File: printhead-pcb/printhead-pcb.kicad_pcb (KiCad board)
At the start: 2 copper layers, 35 x 35 mm, 61 parts, among them J1 PWR, J10 BL_TOUCH, J2 FAN0, J3 FAN2, J4 FAN1, J5 FAN3, J6 T0, J7 T1, J8 T2, J9 T3, Q1 DTC143E, Q2 DTC143E, Q3 DTC143E, Q4 DTC143E, U1 EMC2302-2-AIZL-TR, U2 EMC2302-2-AIZL-TR, U3 ADS1015IDGS, U4 PCA9536D

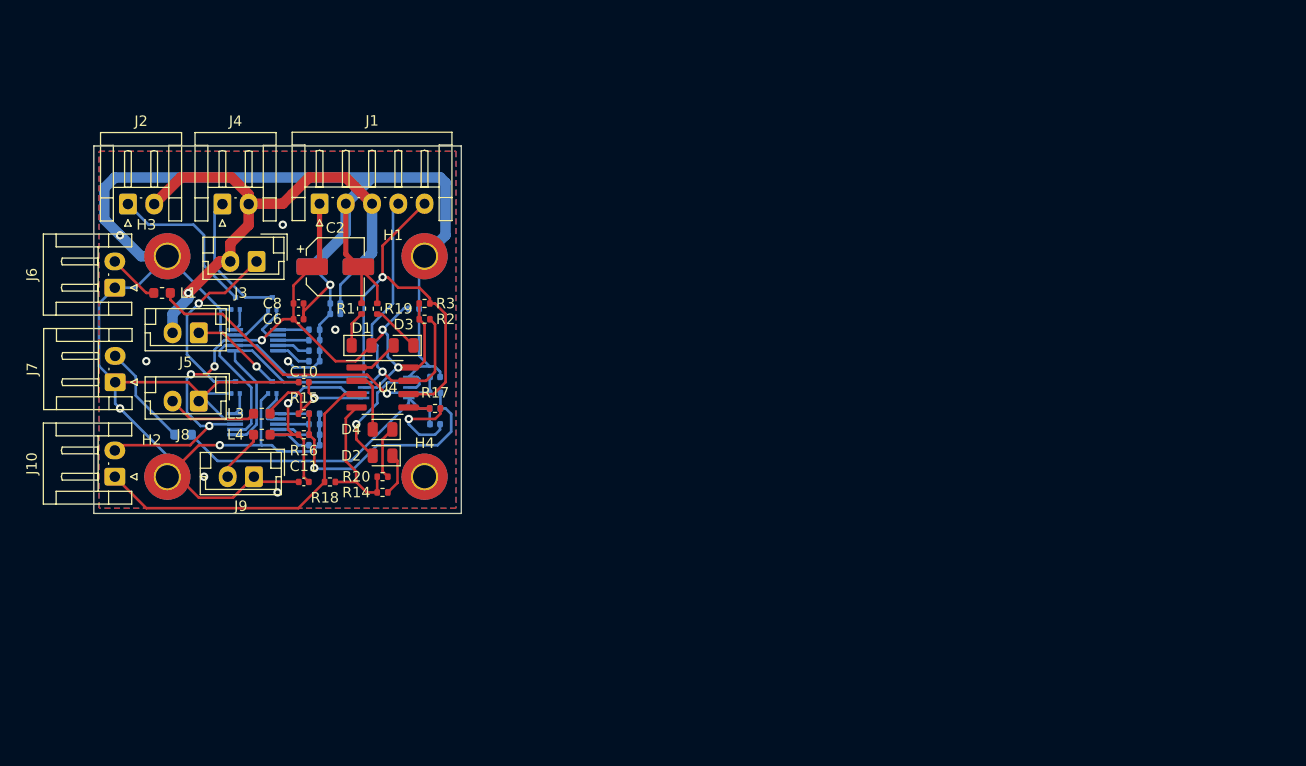
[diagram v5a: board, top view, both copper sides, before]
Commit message: removed led driver, added RJ45 (data connector), fan 3. 4. on off
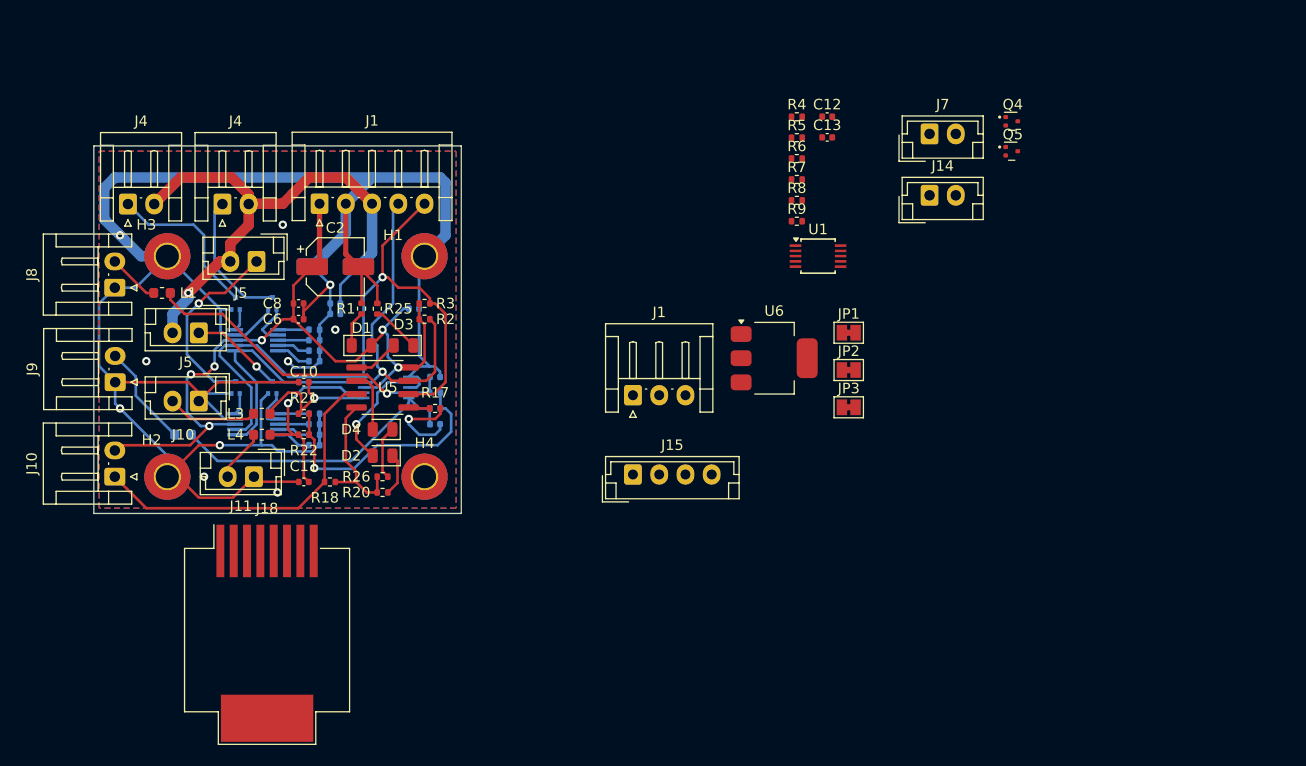
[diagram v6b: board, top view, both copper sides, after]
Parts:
- added C12: 4.7µF, Capacitor_SMD:C_0402_1005Metric, F.Cu at (176.3, 45.7)
- added C13: 4.7µF, Capacitor_SMD:C_0402_1005Metric, F.Cu at (176.3, 47.7)
- added J1: Power, Connector_JST:JST_EH_S3B-EH_1x03_P2.50mm_Horizontal, F.Cu at (157.8, 72.2)
- added J14: FAN4, Connector_JST:JST_EH_B2B-EH-A_1x02_P2.50mm_Vertical, F.Cu at (186.1, 53.2)
- added J15: BreakoutBoardADXL345, Connector_JST:JST_EH_B4B-EH-A_1x04_P2.50mm_Vertical, F.Cu at (157.8, 79.8)
- added J18: DATA, Connector_RJ:RJ45_Molex_0855135013_Vertical, F.Cu at (123.0, 94.9)
- added J7: FAN3, Connector_JST:JST_EH_B2B-EH-A_1x02_P2.50mm_Vertical, F.Cu at (186.1, 47.4)
- added JP1: MEASO, Jumper:SolderJumper-2_P1.3mm_Bridged_Pad1.0x1.5mm, F.Cu at (178.4, 66.3)
- added JP2: MEASO, Jumper:SolderJumper-2_P1.3mm_Bridged_Pad1.0x1.5mm, F.Cu at (178.4, 69.8)
- added JP3: MEASO, Jumper:SolderJumper-2_P1.3mm_Bridged_Pad1.0x1.5mm, F.Cu at (178.4, 73.4)
- added Q4: DTC143E, Package_TO_SOT_SMD:SOT-723, F.Cu at (193.9, 46.1)
- added Q5: DTC143E, Package_TO_SOT_SMD:SOT-723, F.Cu at (193.9, 49.0)
- added R4: 600, Resistor_SMD:R_0402_1005Metric, F.Cu at (173.5, 45.7)
- added R5: 120, Resistor_SMD:R_0402_1005Metric, F.Cu at (173.5, 47.7)
- added R6: 600, Resistor_SMD:R_0402_1005Metric, F.Cu at (173.5, 49.7)
- added R7: 600, Resistor_SMD:R_0402_1005Metric, F.Cu at (173.5, 51.7)
- added R8: 120, Resistor_SMD:R_0402_1005Metric, F.Cu at (173.5, 53.7)
- added R9: 600, Resistor_SMD:R_0402_1005Metric, F.Cu at (173.5, 55.7)
- added U1: PCA9615DP, Package_SO:TSSOP-10_3x3mm_P0.5mm, F.Cu at (175.5, 59.0)
- added U6: AP7361C-33E, Package_TO_SOT_SMD:SOT-223-3_TabPin2, F.Cu at (171.3, 68.7)
- R10: renamed from R4; value 10k -> 4k7
- R14: renamed from R8; value 10k -> 4k7
- R16: renamed from R10; value 10k -> 4k7
- R2, R3: value 10k -> 4k7
- renumbered J8 to J10, J9 to J11, J2 to J4, J3 to J5, J6 to J8, J7 to J9, R6 to R12, R12 to R18, R13 to R19, R14 to R20, R15 to R21, R16 to R22, R19 to R25, R20 to R26, U1 to U2, U3 to U4, U4 to U5
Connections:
- C2 pad 1: +3V3 -> +5V
- C4 pad 1: +3V3 -> +5V
- C6 pad 1: +3V3 -> +5V
- C8 pad 1: +3V3 -> +3.3V
- D1 pad 2: +3V3 -> +5V
- J10 pad 2: TC2 -> ADC2
- J11 pad 2: TC3 -> ADC3
- J4 pad 1: Net-(J2-Pin_1) -> Net-(J4-Pin_1)
- J5 pad 1: Net-(J3-Pin_1) -> Net-(J5-Pin_1)
- J8 pad 2: TC0 -> ADC0
- J9 pad 2: TC1 -> ADC1
- Q1 pad 3: Net-(J2-Pin_1) -> Net-(J4-Pin_1)
- Q2 pad 1: FAN_2_PWM -> FAN_1_PWM
- Q2 pad 3: Net-(J3-Pin_1) -> Net-(J5-Pin_1)
- R10 pad 1: Net-(U1-TACH1) -> Net-(U2-TACH1)
- R12 pad 1: Net-(U1-*ALERT) -> Net-(U2-*ALERT)
- R14 pad 1: Net-(U1-TACH2) -> Net-(U2-TACH2)
- R16 pad 1: Net-(U1-CLK) -> Net-(U2-CLK)
- R2 pad 1: +3V3 -> +5V
- R3 pad 1: +3V3 -> +5V
- U2 pad 10: Net-(U1-*ALERT) -> Net-(U2-*ALERT)
- U2 pad 6: Net-(U1-TACH1) -> Net-(U2-TACH1)
- U2 pad 8: Net-(U1-TACH2) -> Net-(U2-TACH2)
- U2 pad 9: Net-(U1-CLK) -> Net-(U2-CLK)
- U4 pad 8: +3V3 -> +3.3V
- U5 pad 8: +3V3 -> +3.3V
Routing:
- net Net-(J5-Pin_1): track 8.92 -> 27.1 mm, vias 1 -> 2
- net Net-(J3-Pin_1): track 18.2 -> 0.00 mm, vias 1 -> 0
- net Net-(J4-Pin_1): track 13.0 -> 28.6 mm
- net Net-(J2-Pin_1): track 15.6 -> 0.00 mm
- net Net-(U2-*ALERT): track 3.36 -> 6.72 mm
- net Net-(U1-*ALERT): track 3.36 -> 0.00 mm
- net Net-(U2-CLK): track 3.15 -> 6.30 mm
- net Net-(U1-CLK): track 3.15 -> 0.00 mm
- net Net-(U2-TACH1): track 2.95 -> 5.89 mm
- net Net-(U1-TACH1): track 2.95 -> 0.00 mm
- net Net-(U2-TACH2): track 2.95 -> 5.89 mm
- net Net-(U1-TACH2): track 2.95 -> 0.00 mm

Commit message: implemented custom footprint
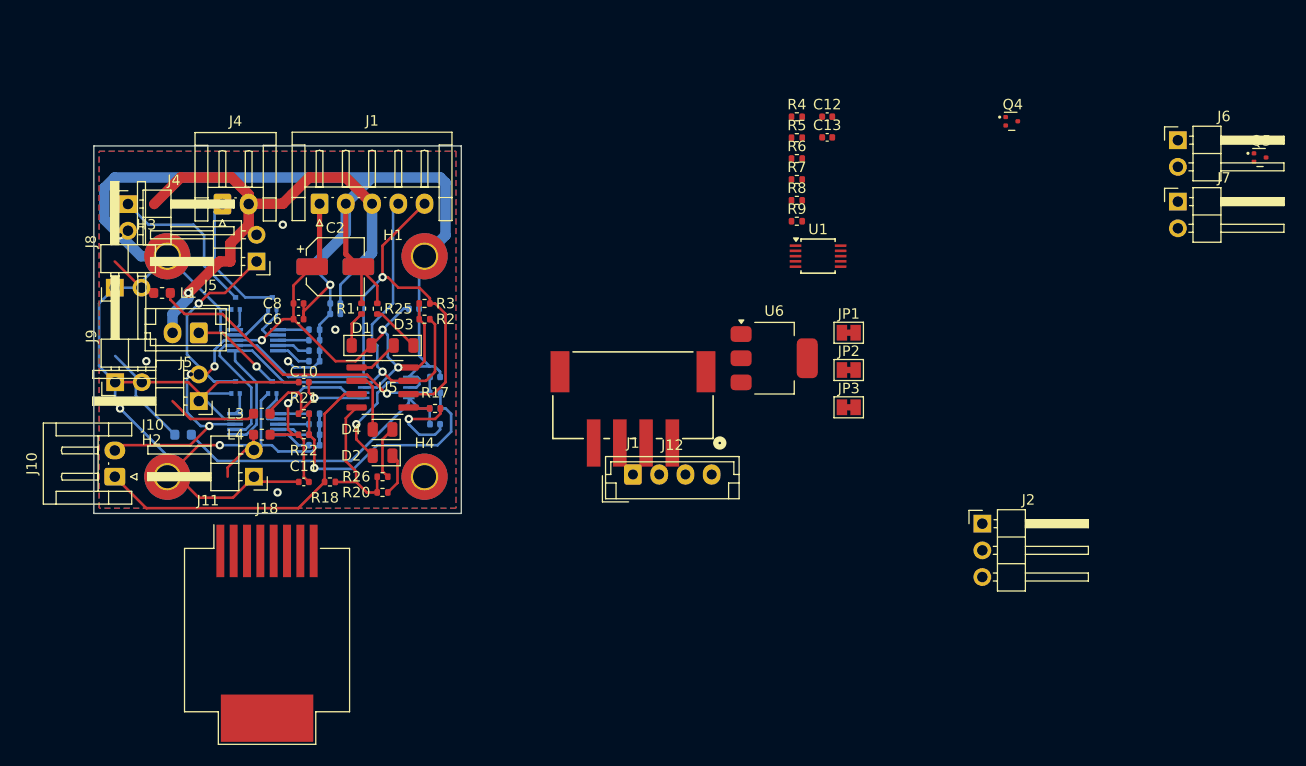
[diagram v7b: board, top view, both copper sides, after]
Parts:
- added J2: Fan_12/5V_Regelung, Connector_PinHeader_2.54mm:PinHeader_1x03_P2.54mm_Horizontal, F.Cu at (191.1, 84.5)
- C10: value 0.1µFC -> 0.1µF
- J1: footprint Connector_JST:JST_EH_S3B-EH_1x03_P2.50mm_Horizontal -> CustomFotLibByJan:CONN4_S4B-XH_JST
- J10, J11: footprint Connector_JST:JST_EH_B2B-EH-A_1x02_P2.50mm_Vertical -> Connector_PinHeader_2.54mm:PinHeader_1x02_P2.54mm_Horizontal
- J12: renamed from J15; value BreakoutBoardADXL345 -> Breakout_Board_ADXL345
- J4, J8, J9: footprint Connector_JST:JST_EH_S2B-EH_1x02_P2.50mm_Horizontal -> Connector_PinHeader_2.54mm:PinHeader_1x02_P2.54mm_Horizontal
- J5: value FAN2 -> FAN1; footprint Connector_JST:JST_EH_B2B-EH-A_1x02_P2.50mm_Vertical -> Connector_PinHeader_2.54mm:PinHeader_1x02_P2.54mm_Horizontal
- J6: renamed from J7; value FAN3 -> FAN2; footprint Connector_JST:JST_EH_B2B-EH-A_1x02_P2.50mm_Vertical -> Connector_PinHeader_2.54mm:PinHeader_1x02_P2.54mm_Horizontal
- J7: renamed from J14; footprint Connector_JST:JST_EH_B2B-EH-A_1x02_P2.50mm_Vertical -> Connector_PinHeader_2.54mm:PinHeader_1x02_P2.54mm_Horizontal
- moved J6 23.7 mm to (209.8, 48.0)
- moved J7 23.7 mm to (209.8, 53.8)
- moved Q5 23.7 mm to (217.6, 49.6)
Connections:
- J4 pad 2: +12V -> Fan_Versorgung
- J5 pad 2: +12V -> Fan_Versorgung
- J6 pad 2: +12V -> Fan_Versorgung
- J7 pad 2: +12V -> Fan_Versorgung

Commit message: added new sheet for stacked pcb
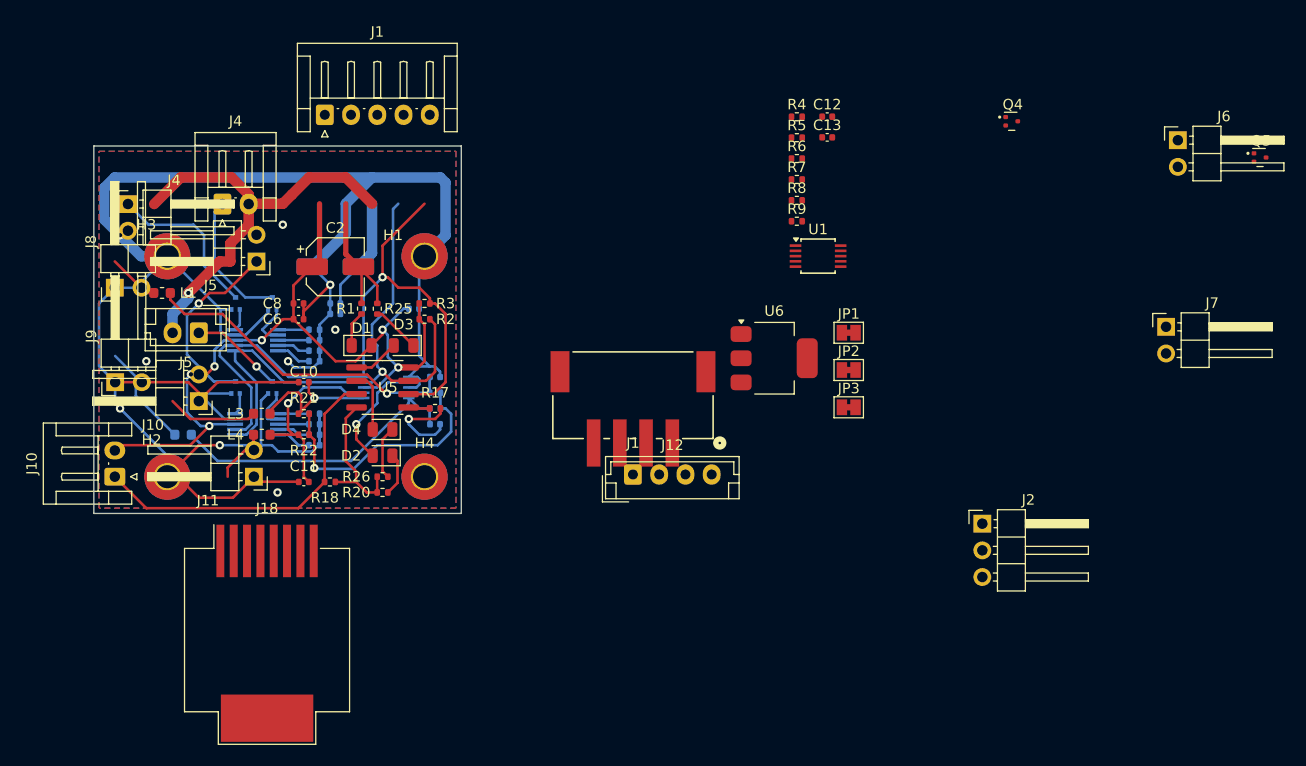
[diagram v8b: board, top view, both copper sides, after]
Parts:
- moved J7 12.0 mm to (208.6, 65.7)
- moved J1 8.48 mm to (128.5, 45.5)
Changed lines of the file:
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@@
 	(footprint "Connector_PinHeader_2.54mm:PinHeader_1x02_P2.54mm_Horizontal"
 		(layer "F.Cu")
-		(at 209.75 53.8)
+		(at 208.625 65.725)
 		(descr "Through hole angled pin header, 1x02, 2.54mm pitch, 6mm pin length, single row")
 		(tags "Through hole angled pin header THT 1x02 2.54mm single row")
@@
 	(footprint "Connector_JST:JST_EH_S5B-EH_1x05_P2.50mm_Horizontal"
 		(layer "F.Cu")
-		(at 128 54)
+		(at 128.5 45.5325)
 		(descr "JST EH series connector, S5B-EH (http://www.jst-mfg.com/product/pdf/eng/eEH.pdf), generated with kicad-footprint-generator")
 		(tags "connector JST EH horizontal")
